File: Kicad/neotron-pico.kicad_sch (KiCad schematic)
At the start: 26 parts, among them J101 Neotron-Expansion-Slot, J102 Neotron-Expansion-Slot, J103 Neotron-Expansion-Slot, J104 Conn_01x09, J105 Neotron-Expansion-Slot, J106 Conn_01x06_Pins, J107 Conn_01x09, J108 Conn_01x09, Q101 DMG2305UX, U101 Pico

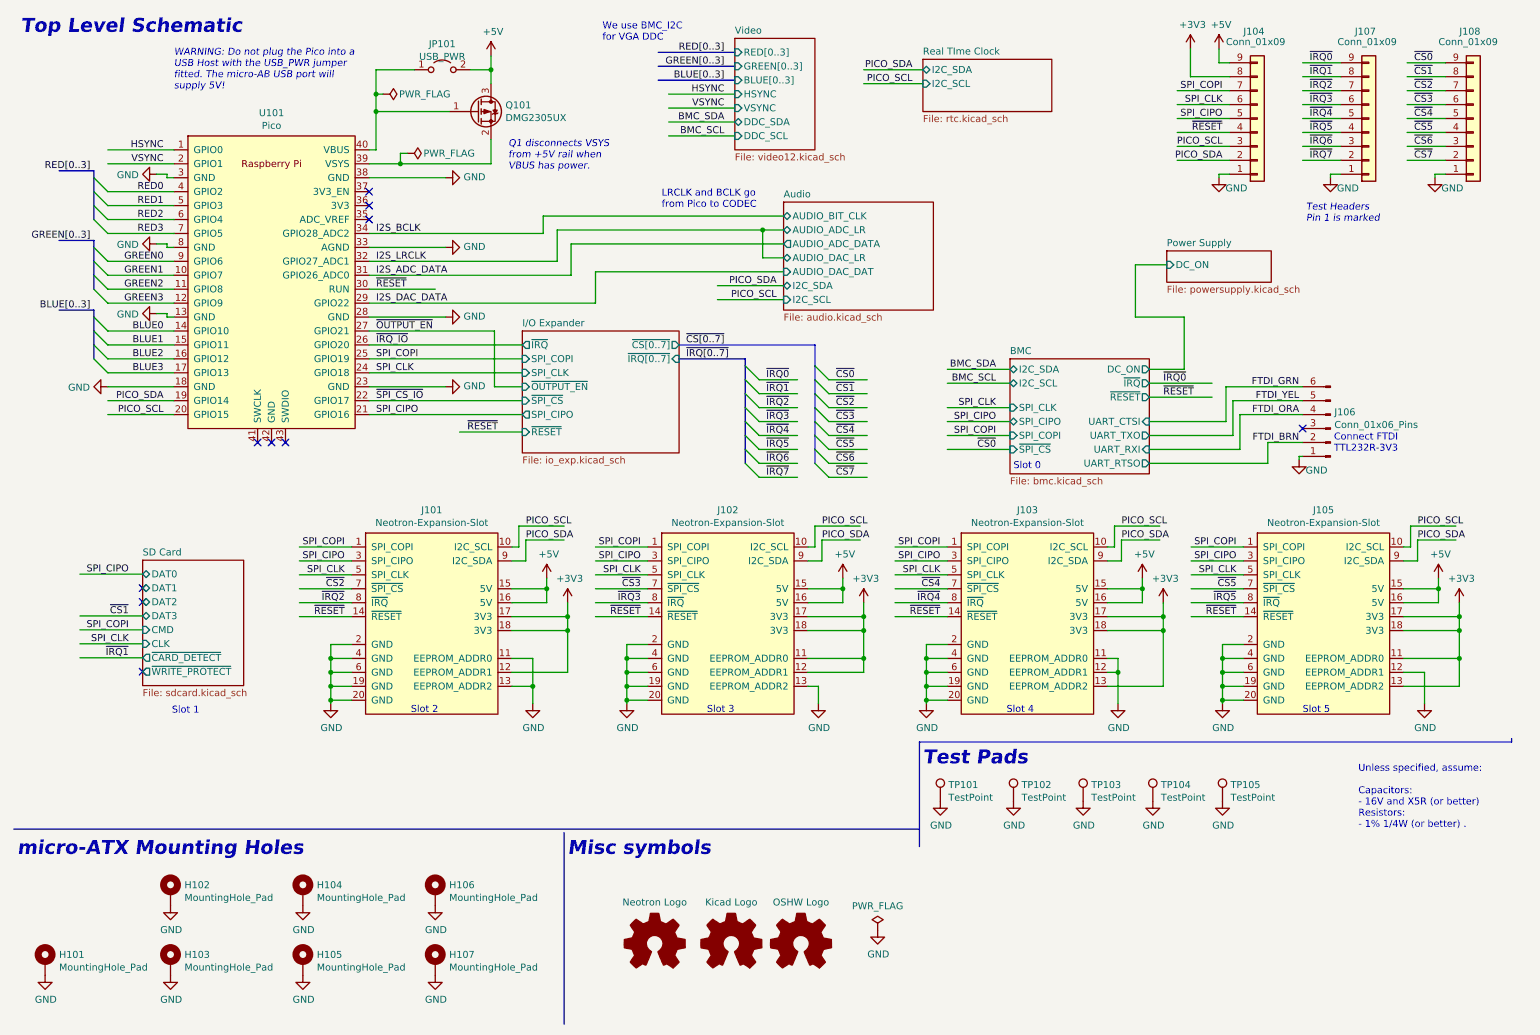
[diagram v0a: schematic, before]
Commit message: Add I2C pull-ups.
Also revised the Neotron Pico symbol to put all the GPIO on one side
and all the GND at the bottom.

Closes: #61
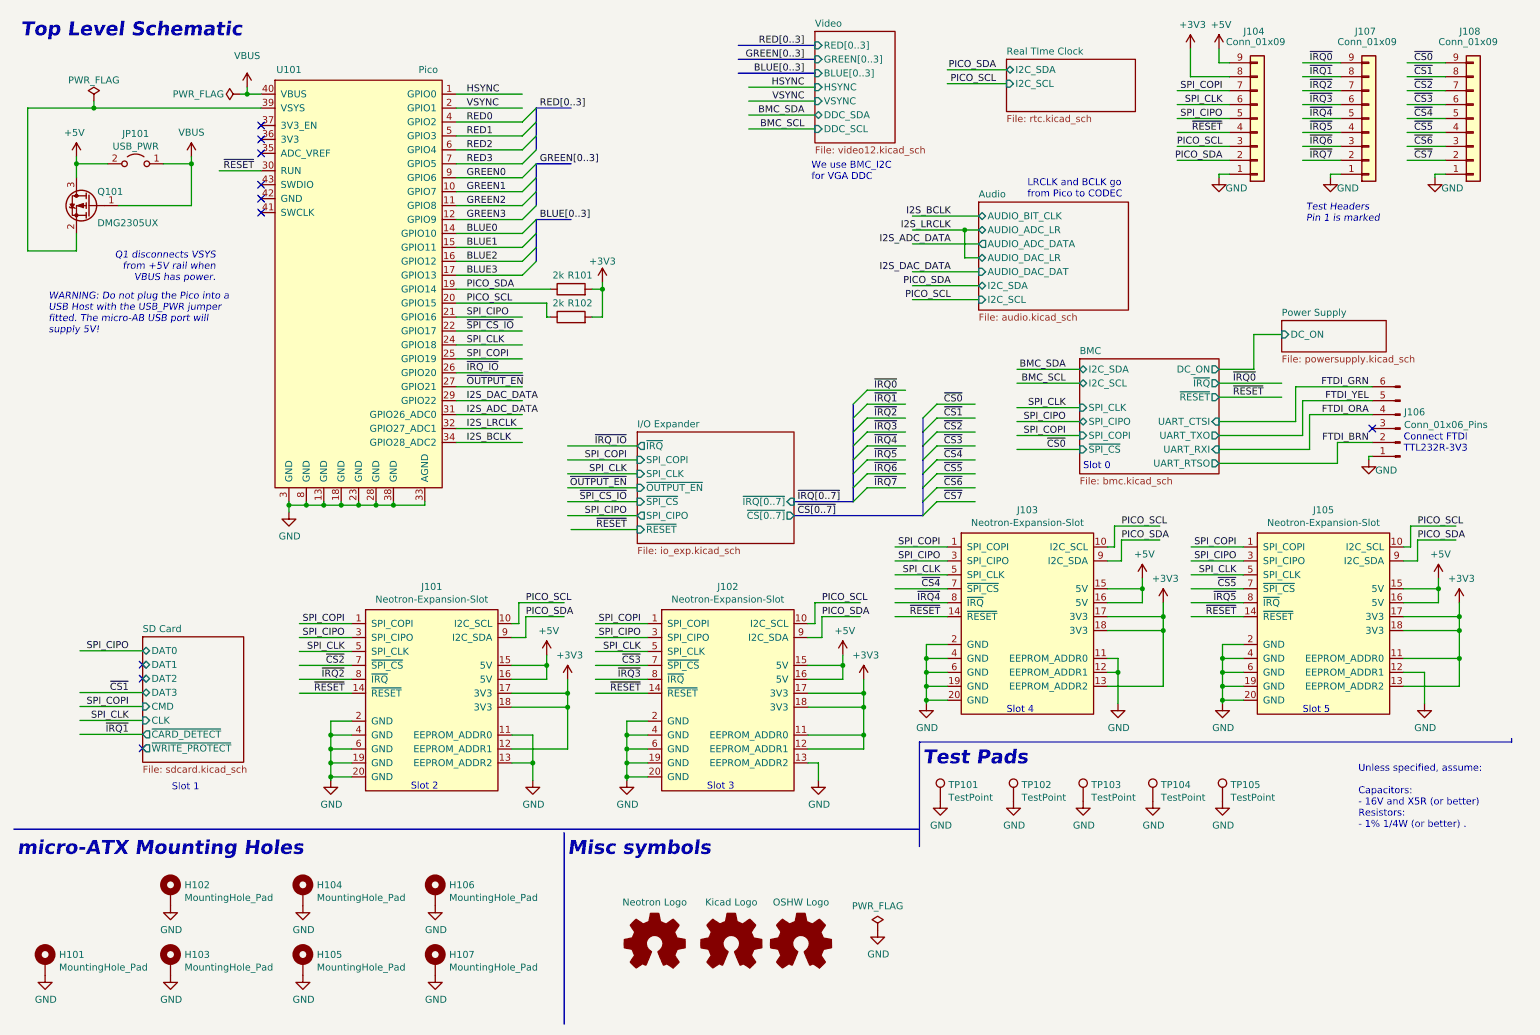
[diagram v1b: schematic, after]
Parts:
- added R101, R102: 2k, Resistor_SMD:R_0805_2012Metric_Pad1.20x1.40mm_HandSolder, symbol Device:R
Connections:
- net +3V3: now also R101.2, R102.2
- net PICO_SCL: now also R102.1
- net PICO_SDA: now also R101.1
- net VBUS: now reaches JP101.1 (A), Q101.1 (G), U101.40 (VBUS)
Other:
- moved on the sheet: J101, J102, J106, JP101, Q101

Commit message: Removed all CPL parts, and changed standby PSU.
The Holtek was a SOT-89 that had a completely different pinout to
every other SOT-89 3.3V LDO out there. To avoid confusion I
wanted to replace it, but the only other basic JLCPCB parts
were the AMS1117 (huge quiescent current) and something only
rated to 7V input voltage (this LDO gets the full VDC in).

So, I used a TO-92 footprint and picked an LP2950N.

This, however, needs some ESR on the output cap, so I made
that a 2.2uF electrolytic.

I also removed the 2x 10uF output caps on the K7805 and set
just one 22uF as specified in the datasheet.
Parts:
- J106: value Conn_01x06_Pins -> Conn_01x06
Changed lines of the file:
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@@
       (effects (font (size 1.27 1.27)) (justify right))
     )
-    (property "Value" "Conn_01x06_Pins" (id 1) (at 265.5062 88.8492 0)
+    (property "Value" "Conn_01x06" (id 1) (at 265.5062 88.8492 0)
       (effects (font (size 1.27 1.27)) (justify right))
     )
@@
   (symbol (lib_id "power:GND") (at 62.23 104.775 0) (unit 1)
     (in_bom yes) (on_board yes)
-    (property "Reference" "#PWR?" (id 0) (at 62.23 111.125 0)
+    (property "Reference" "#PWR0102" (id 0) (at 62.23 111.125 0)
       (effects (font (size 1.27 1.27)) hide)
     )
@@
   (symbol (lib_id "power:VBUS") (at 44.45 40.005 0) (unit 1)
     (in_bom yes) (on_board yes)
-    (property "Reference" "#PWR?" (id 0) (at 44.45 43.815 0)
+    (property "Reference" "#PWR0103" (id 0) (at 44.45 43.815 0)
       (effects (font (size 1.27 1.27)) hide)
     )
@@
   (symbol (lib_id "power:VBUS") (at 54.61 27.305 0) (unit 1)
     (in_bom yes) (on_board yes) (fields_autoplaced)
-    (property "Reference" "#PWR?" (id 0) (at 54.61 31.115 0)
+    (property "Reference" "#PWR0104" (id 0) (at 54.61 31.115 0)
       (effects (font (size 1.27 1.27)) hide)
     )
@@
       (reference "#PWR0101") (unit 1) (value "GND") (footprint "")
     )
+    (path "/0692467e-4d98-4b5f-909e-64be65758f3b"
+      (reference "#PWR0102") (unit 1) (value "GND") (footprint "")
+    )
+    (path "/33517fd8-bfa1-4c4f-a8e6-e9d782d16a8b"
+      (reference "#PWR0103") (unit 1) (value "VBUS") (footprint "")
+    )
+    (path "/439a13c1-0f1f-40f7-9a4b-6f5d52b6137e"
+      (reference "#PWR0104") (unit 1) (value "VBUS") (footprint "")
+    )
     (path "/00000000-0000-0000-0000-000060b3dfa1"
       (reference "#PWR0106") (unit 1) (value "GND") (footprint "")
@@
       (reference "#PWR01112") (unit 1) (value "GND") (footprint "")
     )
-    (path "/0692467e-4d98-4b5f-909e-64be65758f3b"
-      (reference "#PWR?") (unit 1) (value "GND") (footprint "")
-    )
-    (path "/33517fd8-bfa1-4c4f-a8e6-e9d782d16a8b"
-      (reference "#PWR?") (unit 1) (value "VBUS") (footprint "")
-    )
-    (path "/439a13c1-0f1f-40f7-9a4b-6f5d52b6137e"
-      (reference "#PWR?") (unit 1) (value "VBUS") (footprint "")
-    )
     (path "/00000000-0000-0000-0000-00005fef404d/00000000-0000-0000-0000-00005e0f507e"
       (reference "BT801") (unit 1) (value "CR2032") (footprint "Neotron-Common-Hardware:BatteryHolder_Keystone_103_1x20mm")
@@
     )
     (path "/00000000-0000-0000-0000-00005fde7599/930a8dcf-4cce-46ee-a662-11ce8573edbf"
-      (reference "C1103") (unit 1) (value "10uF") (footprint "Capacitor_SMD:C_0805_2012Metric_Pad1.18x1.45mm_HandSolder")
+      (reference "C1103") (unit 1) (value "1uF") (footprint "Capacitor_SMD:C_0805_2012Metric_Pad1.18x1.45mm_HandSolder")
     )
     (path "/00000000-0000-0000-0000-00005fde7599/00000000-0000-0000-0000-0000606e29db"
-      (reference "C1104") (unit 1) (value "10uF") (footprint "Capacitor_SMD:C_0805_2012Metric_Pad1.18x1.45mm_HandSolder")
+      (reference "C1104") (unit 1) (value "22uF") (footprint "Capacitor_SMD:C_0805_2012Metric_Pad1.18x1.45mm_HandSolder")
     )
     (path "/00000000-0000-0000-0000-00005fde7599/7aa4c31a-c7d2-40c3-be15-ff4382a68fc6"
-      (reference "C1105") (unit 1) (value "10uF") (footprint "Capacitor_SMD:C_0805_2012Metric_Pad1.18x1.45mm_HandSolder")
-    )
-    (path "/00000000-0000-0000-0000-00005fde7599/00000000-0000-0000-0000-000060e7e52a"
-      (reference "C1106") (unit 1) (value "10uF") (footprint "Capacitor_SMD:C_0805_2012Metric_Pad1.18x1.45mm_HandSolder")
+      (reference "C1105") (unit 1) (value "2.2uF") (footprint "Capacitor_SMD:CP_Elec_4x5.4")
     )
     (path "/00000000-0000-0000-0000-00005fde7599/00000000-0000-0000-0000-0000606e29ce"
@@
     )
     (path "/00000000-0000-0000-0000-0000607e546b"
-      (reference "J106") (unit 1) (value "Conn_01x06_Pins") (footprint "Connector_PinHeader_2.54mm:PinHeader_1x06_P2.54mm_Vertical")
+      (reference "J106") (unit 1) (value "Conn_01x06") (footprint "Connector_PinHeader_2.54mm:PinHeader_1x06_P2.54mm_Vertical")
     )
     (path "/00000000-0000-0000-0000-000060bff553"
@@
     )
     (path "/00000000-0000-0000-0000-00005fde7599/8e44377e-becb-4620-a243-a1d7822574c8"
-      (reference "U1102") (unit 1) (value "HT7533-1-SOT89") (footprint "Package_TO_SOT_SMD:SOT-89-3")
+      (reference "U1102") (unit 1) (value "LP2950N") (footprint "Package_TO_SOT_THT:TO-92_Inline")
     )
     (path "/00000000-0000-0000-0000-00005fde7599/00000000-0000-0000-0000-00005fece573"

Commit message: LED and Switch updates.
Case LEDs are now driven by VDC and 1K. Allows higher Vf LEDs to work.
Added 6mm buttons.
Fiddled with tracking around CODEC.
Change I2S pin ordering.

Closes: #42 #60 #46
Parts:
- renumbered J107 to J106, J106 to J107
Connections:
- net I2S_ADC_DATA: now also U101.29 (GPIO22); no longer U101.31 (GPIO26_ADC0)
- net I2S_BCLK: now also U101.32 (GPIO27_ADC1); no longer U101.34 (GPIO28_ADC2)
- net I2S_DAC_DATA: now also U101.31 (GPIO26_ADC0); no longer U101.29 (GPIO22)
- net I2S_LRCLK: now also U101.34 (GPIO28_ADC2); no longer U101.32 (GPIO27_ADC1)
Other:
- note added: "Unless specified, assume: Capacitors: - 16V and X5R (or better) Resistors: - 1% 1/8W (or better) ."
- note removed: "Unless specified, assume: Capacitors: - 16V and X5R (or better) Resistors: - 1% 1/4W (or better) ."
- moved on the sheet: JP101, Q101, R101, R102, U101

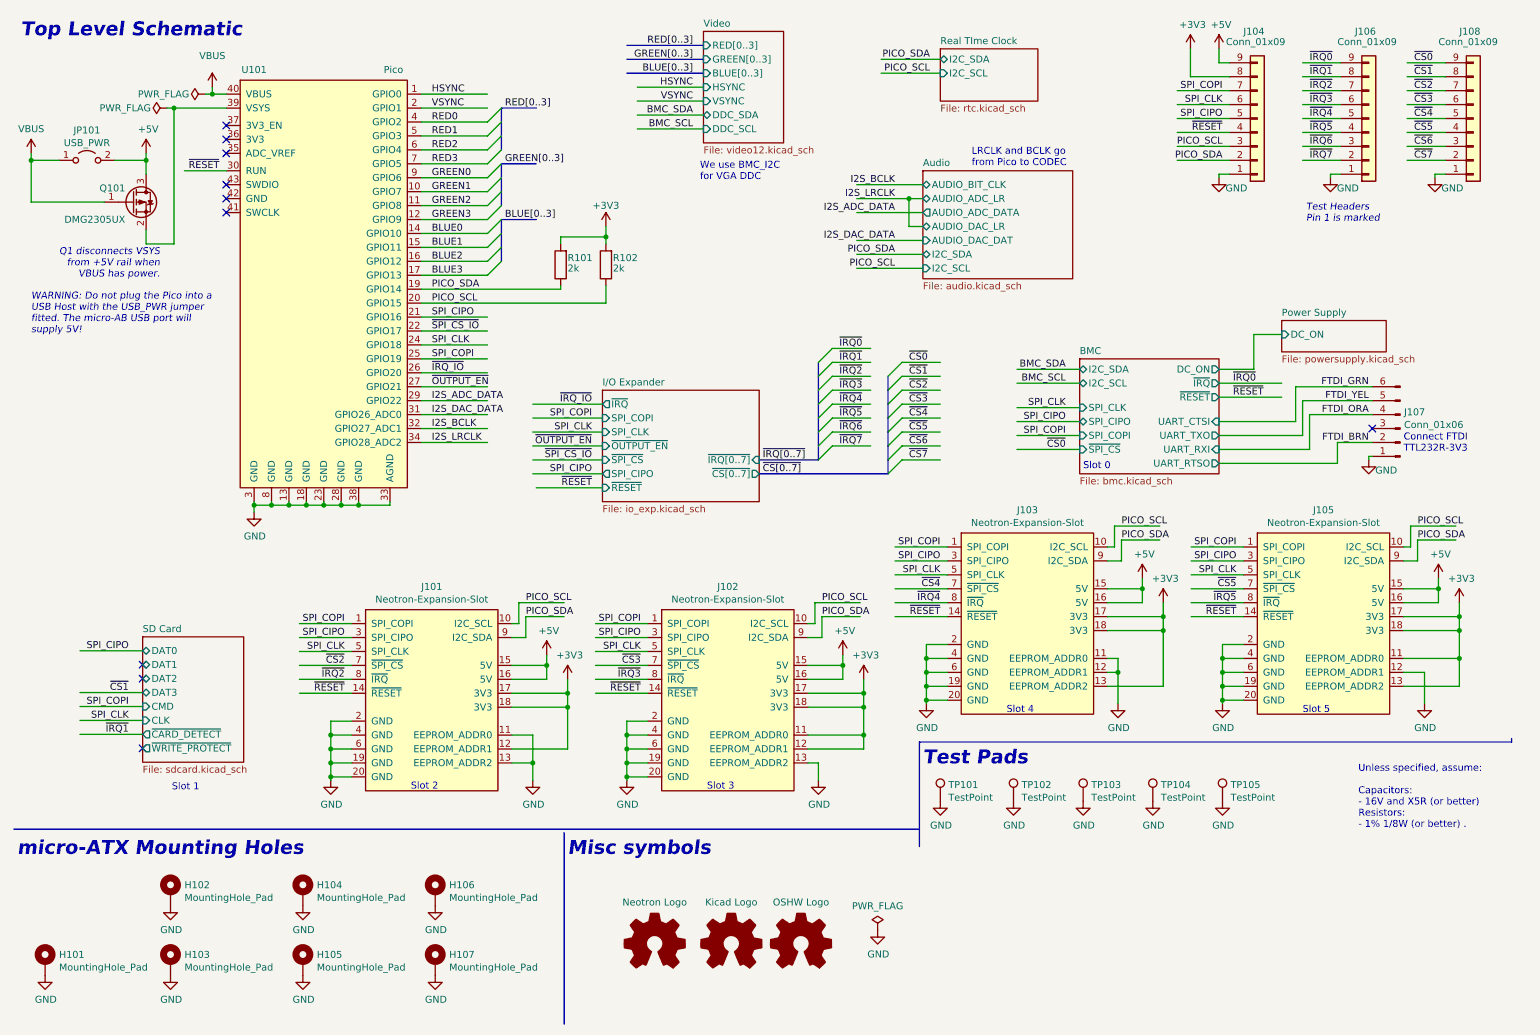
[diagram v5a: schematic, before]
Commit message: Re-organised top sheet.
Lots of parts just changed their component designator. I had
to patch up the PCB manually, but now it imports from the schematic
OK.

Also adds two PSU rails for the RTC (so you can pick DS1307
which is a 5V part, or MCP7940N which is a 3.3V part).
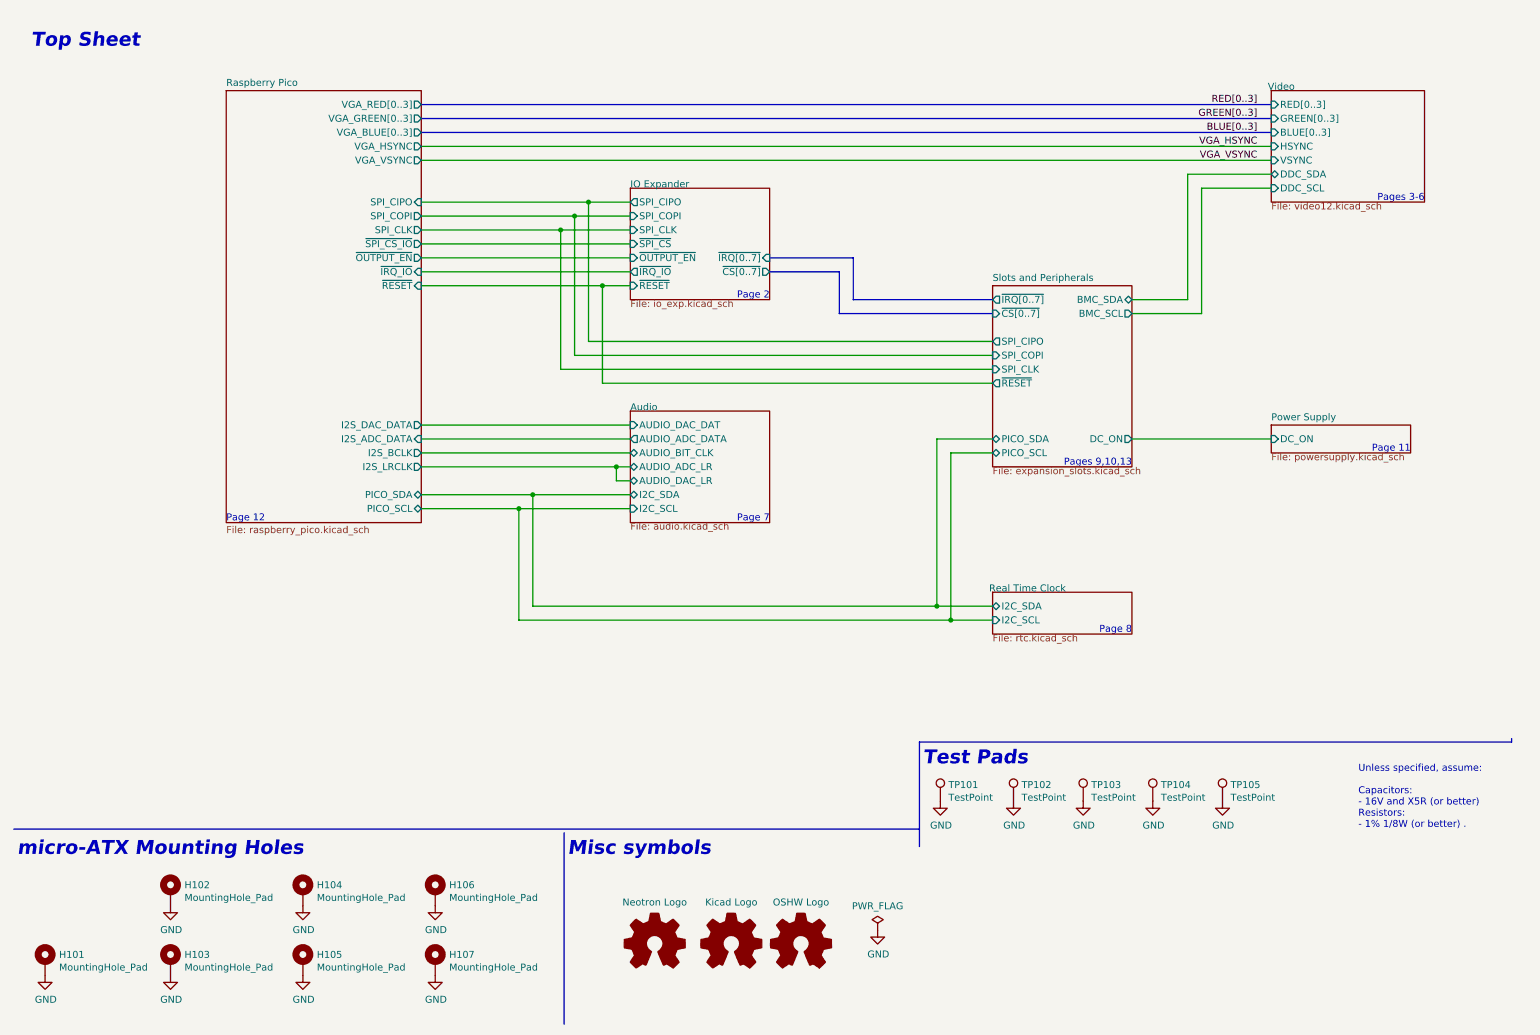
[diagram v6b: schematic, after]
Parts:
- removed J101, J102, J103, J105: Neotron-Expansion-Slot, Neotron-Common-Hardware:Neotron-Expansion-Slot, symbol Neotron-Common-Hardware:Neotron-Expansion-Slot
- removed J104, J106, J108: Conn_01x09, Connector_PinHeader_2.54mm:PinHeader_1x09_P2.54mm_Vertical, symbol Connector_Generic:Conn_01x09
- removed J107: Conn_01x06, Connector_PinHeader_2.54mm:PinHeader_1x06_P2.54mm_Vertical, symbol Connector:Conn_01x06_Male
- removed JP101: USB_PWR, Connector_PinHeader_2.54mm:PinHeader_1x02_P2.54mm_Vertical, symbol Jumper:Jumper_2_Open
- removed Q101: DMG2305UX, Package_TO_SOT_SMD:SOT-23, symbol Device:Q_PMOS_GSD
- removed R101, R102: 2k, Resistor_SMD:R_0805_2012Metric_Pad1.20x1.40mm_HandSolder, symbol Device:R
- removed U101: Pico, RPi_Pico:RPi_Pico_SMD_TH, symbol neotron-pico:Raspberry_Pi_Pico
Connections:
- no-connect marks 10 -> 0
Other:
- sheet I/O Expander renamed IO Expander
- sheet Real TIme Clock renamed Real Time Clock
- removed sheet BMC
- removed sheet SD Card
- added sheet Raspberry Pico (raspberry_pico.kicad_sch)
- added sheet Slots and Peripherals (expansion_slots.kicad_sch)
- sheet IO Expander ports: added ~{IRQ_IO}; removed ~{IRQ}
- note added: "Page 11"
- note added: "Page 12"
- note added: "Page 2"
- note added: "Page 7"
- note added: "Page 8"
- note added: "Pages 3-6"
- note added: "Pages 9,10,13"
- note added: "Top Sheet"
- note removed: "Connect FTDI TTL232R-3V3"
- note removed: "LRCLK and BCLK go from Pico to CODEC"
- note removed: "Q1 disconnects VSYS from +5V rail when VBUS has power."
- note removed: "Slot 0"
- note removed: "Slot 1"
- note removed: "Slot 2"
- note removed: "Slot 3"
- note removed: "Slot 4"
- note removed: "Slot 5"
- note removed: "Test Headers Pin 1 is marked"
- note removed: "Top Level Schematic"
- note removed: "WARNING: Do not plug the Pico into a USB Host with the USB_PWR jumper fitted. The micro-AB USB port will supply 5V!"
- note removed: "We use BMC_I2C for VGA DDC"
